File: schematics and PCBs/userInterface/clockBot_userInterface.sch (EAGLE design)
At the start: 6 parts, among them X1 5566-8

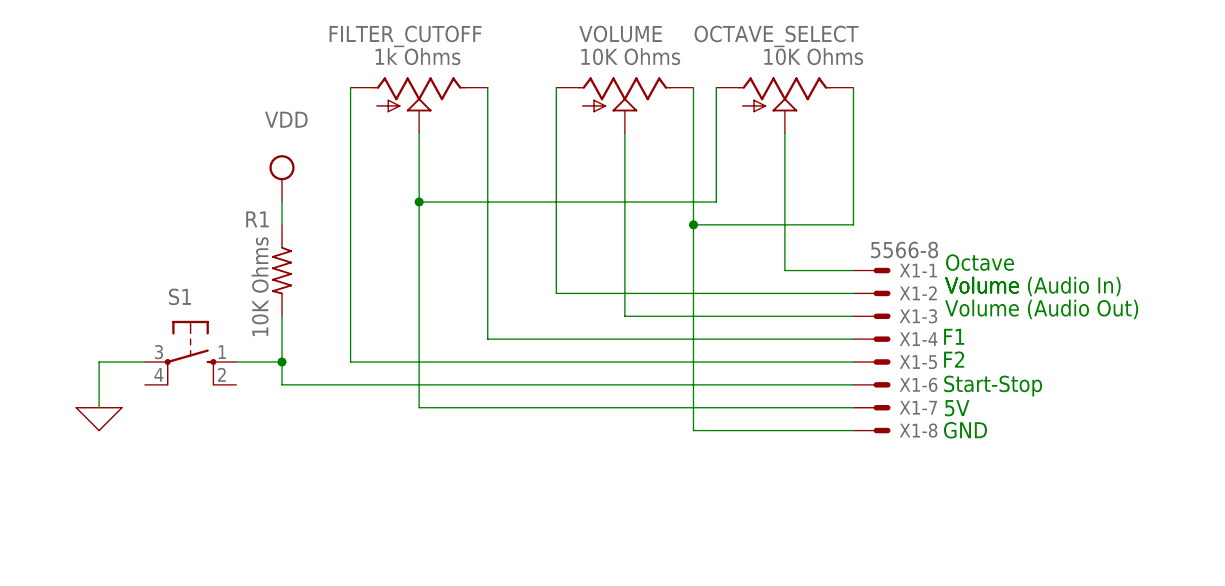
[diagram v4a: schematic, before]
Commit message: User itnerface switch update
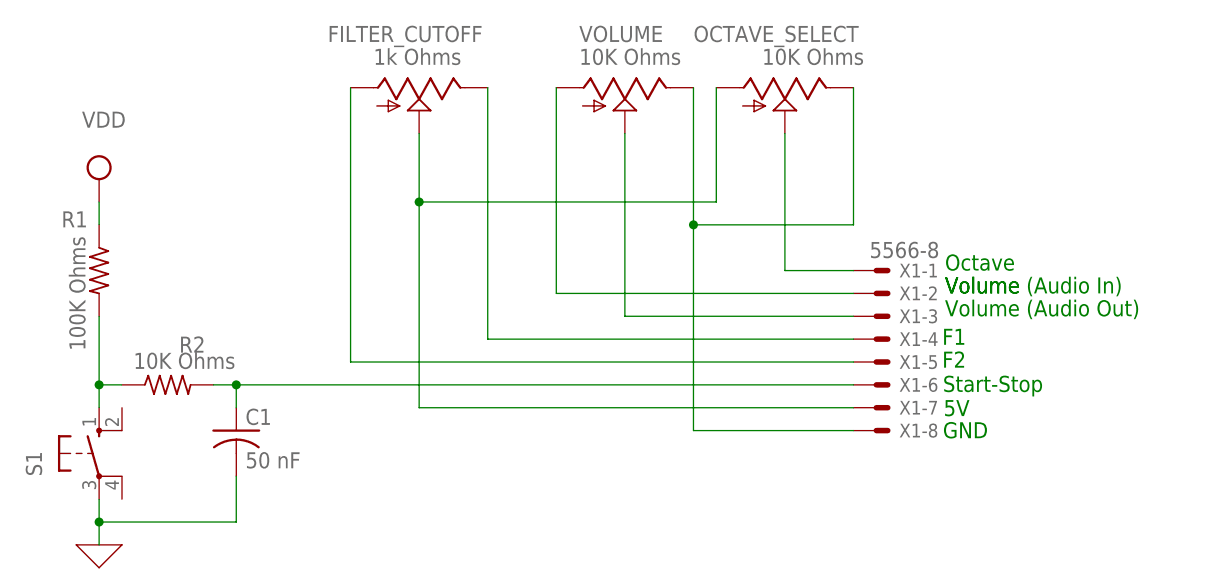
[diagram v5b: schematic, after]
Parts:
- added C1: 50 nF, adafruit:C-US025-025X050
- added R2: 10K Ohms, adafruit:FLIPFLOP-RES
- R1: value 10K Ohms -> 100K Ohms
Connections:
- new net N$7: R1.2, R2.1, S1.S
- net 0: now also C1.2
- net N$1: now also C1.1, R2.2; no longer R1.2, S1.S
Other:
- moved on the sheet: R1, S1
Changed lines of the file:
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@@
 <part name="SUPPLY1" library="supply2" library_urn="urn:adsk.eagle:library:372" deviceset="VDD" device=""/>
 <part name="X_1" library="ngspice-simulation" library_urn="urn:adsk.eagle:library:527439" deviceset="GND" device=""/>
-<part name="R1" library="adafruit" library_urn="urn:adsk.eagle:library:420" deviceset="FLIPFLOP-RES" device="" package3d_urn="urn:adsk.eagle:package:6240726/1" value="10K Ohms"/>
+<part name="R1" library="adafruit" library_urn="urn:adsk.eagle:library:420" deviceset="FLIPFLOP-RES" device="" package3d_urn="urn:adsk.eagle:package:6240726/1" value="100K Ohms"/>
 <part name="X1" library="con-molex" library_urn="urn:adsk.eagle:library:165" deviceset="5566-8" device="" package3d_urn="urn:adsk.eagle:package:8078580/1"/>
 <part name="S1" library="switch-omron" library_urn="urn:adsk.eagle:library:377" deviceset="10-XX" device="" package3d_urn="urn:adsk.eagle:package:27496/1"/>
+<part name="C1" library="adafruit" library_urn="urn:adsk.eagle:library:420" deviceset="C-US" device="025-025X050" package3d_urn="urn:adsk.eagle:package:6240323/1" value="50 nF"/>
+<part name="R2" library="adafruit" library_urn="urn:adsk.eagle:library:420" deviceset="FLIPFLOP-RES" device="" package3d_urn="urn:adsk.eagle:package:6240726/1" value="10K Ohms"/>
 </parts>
 <sheets>
@@
 <attribute name="VALUE" x="60.96" y="63.5" size="1.778" layer="96"/>
 </instance>
-<instance part="SUPPLY1" gate="G$1" x="7.62" y="50.8" smashed="yes">
-<attribute name="VALUE" x="5.715" y="56.515" size="1.778" layer="96"/>
+<instance part="SUPPLY1" gate="G$1" x="-12.7" y="50.8" smashed="yes">
+<attribute name="VALUE" x="-14.605" y="56.515" size="1.778" layer="96"/>
 </instance>
-<instance part="X_1" gate="G$1" x="-12.7" y="25.4" smashed="yes"/>
-<instance part="R1" gate="G$1" x="7.62" y="40.64" smashed="yes" rot="R270">
-<attribute name="NAME" x="6.35" y="47.2186" size="1.778" layer="95" rot="R180"/>
-<attribute name="VALUE" x="4.318" y="44.45" size="1.778" layer="96" rot="R270"/>
+<instance part="X_1" gate="G$1" x="-12.7" y="10.16" smashed="yes"/>
+<instance part="R1" gate="G$1" x="-12.7" y="40.64" smashed="yes" rot="R270">
+<attribute name="NAME" x="-13.97" y="47.2186" size="1.778" layer="95" rot="R180"/>
+<attribute name="VALUE" x="-16.002" y="44.45" size="1.778" layer="96" rot="R270"/>
 </instance>
 <instance part="X1" gate="-1" x="73.66" y="40.64" smashed="yes">
@@
 <attribute name="NAME" x="76.2" y="22.098" size="1.524" layer="95"/>
 </instance>
-<instance part="S1" gate="1" x="-2.54" y="30.48" smashed="yes" rot="R270">
-<attribute name="NAME" x="-5.08" y="36.83" size="1.778" layer="95"/>
-<attribute name="VALUE" x="0.635" y="34.29" size="1.778" layer="96"/>
+<instance part="S1" gate="1" x="-12.7" y="20.32" smashed="yes">
+<attribute name="NAME" x="-19.05" y="17.78" size="1.778" layer="95" rot="R90"/>
+<attribute name="VALUE" x="-16.51" y="23.495" size="1.778" layer="96" rot="R90"/>
+</instance>
+<instance part="C1" gate="G$1" x="2.54" y="22.86" smashed="yes">
+<attribute name="NAME" x="3.556" y="23.495" size="1.778" layer="95"/>
+<attribute name="VALUE" x="3.556" y="18.669" size="1.778" layer="96"/>
+</instance>
+<instance part="R2" gate="G$1" x="-5.08" y="27.94" smashed="yes">
+<attribute name="NAME" x="-3.81" y="31.5214" size="1.778" layer="95"/>
+<attribute name="VALUE" x="-8.89" y="29.718" size="1.778" layer="96"/>
 </instance>
 </instances>
@@
 </segment>
 </net>
-<net name="N$1" class="0">
-<segment>
-<pinref part="R1" gate="G$1" pin="2"/>
-<wire x1="7.62" y1="35.56" x2="7.62" y2="30.48" width="0.1524" layer="91"/>
-<wire x1="2.54" y1="30.48" x2="7.62" y2="30.48" width="0.1524" layer="91"/>
-<pinref part="X1" gate="-6" pin="S"/>
-<wire x1="71.12" y1="27.94" x2="7.62" y2="27.94" width="0.1524" layer="91"/>
-<wire x1="7.62" y1="27.94" x2="7.62" y2="30.48" width="0.1524" layer="91"/>
-<junction x="7.62" y="30.48"/>
-<pinref part="S1" gate="1" pin="S"/>
-</segment>
-</net>
 <net name="N$5" class="0">
 <segment>
@@
 <pinref part="R1" gate="G$1" pin="1"/>
 <pinref part="SUPPLY1" gate="G$1" pin="VDD"/>
-<wire x1="7.62" y1="48.26" x2="7.62" y2="45.72" width="0.1524" layer="91"/>
-</segment>
-</net>
-<net name="0" class="0">
-<segment>
-<wire x1="-12.7" y1="25.4" x2="-12.7" y2="30.48" width="0.1524" layer="91"/>
-<pinref part="X_1" gate="G$1" pin="0"/>
-<wire x1="-7.62" y1="30.48" x2="-12.7" y2="30.48" width="0.1524" layer="91"/>
-<pinref part="S1" gate="1" pin="P"/>
+<wire x1="-12.7" y1="48.26" x2="-12.7" y2="45.72" width="0.1524" layer="91"/>
 </segment>
 </net>
@@
 </segment>
 </net>
+<net name="0" class="0">
+<segment>
+<pinref part="X_1" gate="G$1" pin="0"/>
+<pinref part="S1" gate="1" pin="P"/>
+<wire x1="-12.7" y1="15.24" x2="-12.7" y2="12.7" width="0.1524" layer="91"/>
+<wire x1="-12.7" y1="12.7" x2="2.54" y2="12.7" width="0.1524" layer="91"/>
+<junction x="-12.7" y="12.7"/>
+<wire x1="-12.7" y1="12.7" x2="-12.7" y2="10.16" width="0.1524" layer="91"/>
+<pinref part="C1" gate="G$1" pin="2"/>
+<wire x1="2.54" y1="17.78" x2="2.54" y2="12.7" width="0.1524" layer="91"/>
+</segment>
+</net>
+<net name="N$1" class="0">
+<segment>
+<pinref part="X1" gate="-6" pin="S"/>
+<wire x1="71.12" y1="27.94" x2="2.54" y2="27.94" width="0.1524" layer="91"/>
+<pinref part="C1" gate="G$1" pin="1"/>
+<wire x1="2.54" y1="25.4" x2="2.54" y2="27.94" width="0.1524" layer="91"/>
+<pinref part="R2" gate="G$1" pin="2"/>
+<wire x1="0" y1="27.94" x2="2.54" y2="27.94" width="0.1524" layer="91"/>
+<junction x="2.54" y="27.94"/>
+</segment>
+</net>
+<net name="N$7" class="0">
+<segment>
+<pinref part="R1" gate="G$1" pin="2"/>
+<wire x1="-12.7" y1="35.56" x2="-12.7" y2="27.94" width="0.1524" layer="91"/>
+<pinref part="S1" gate="1" pin="S"/>
+<pinref part="R2" gate="G$1" pin="1"/>
+<wire x1="-12.7" y1="27.94" x2="-12.7" y2="25.4" width="0.1524" layer="91"/>
+<wire x1="-10.16" y1="27.94" x2="-12.7" y2="27.94" width="0.1524" layer="91"/>
+<junction x="-12.7" y="27.94"/>
+</segment>
+</net>

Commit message: User interface single row molex
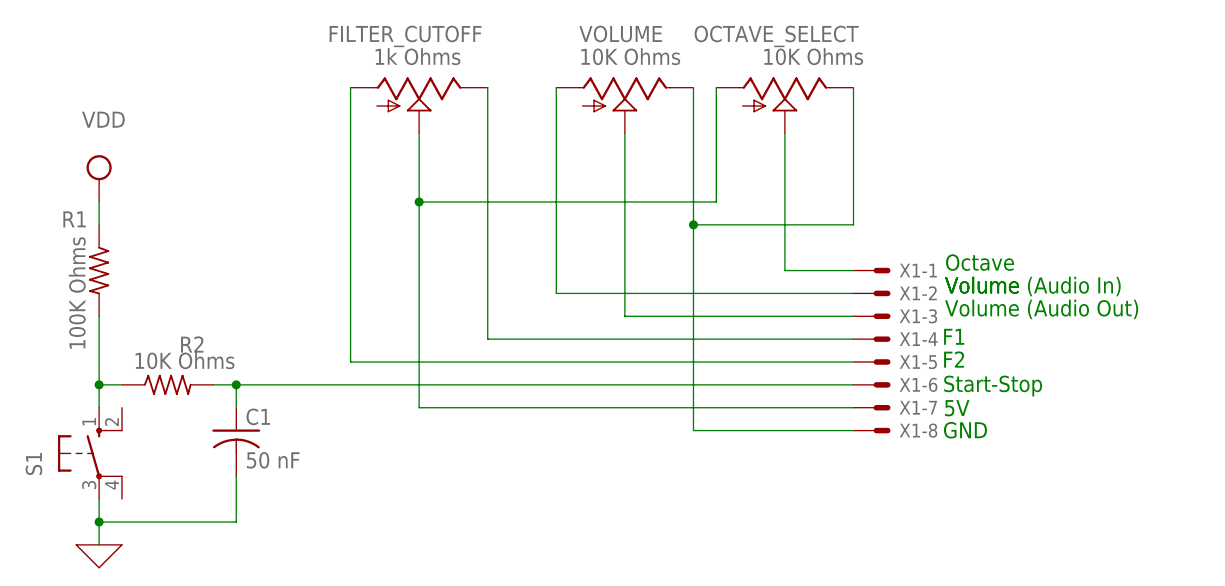
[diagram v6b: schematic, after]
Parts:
- X1: value 5566-8 -> (none); device con-molex:5566-8 -> con-molex:KK-156-8
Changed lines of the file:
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@@
 <part name="X_1" library="ngspice-simulation" library_urn="urn:adsk.eagle:library:527439" deviceset="GND" device=""/>
 <part name="R1" library="adafruit" library_urn="urn:adsk.eagle:library:420" deviceset="FLIPFLOP-RES" device="" package3d_urn="urn:adsk.eagle:package:6240726/1" value="100K Ohms"/>
-<part name="X1" library="con-molex" library_urn="urn:adsk.eagle:library:165" deviceset="5566-8" device="" package3d_urn="urn:adsk.eagle:package:8078580/1"/>
 <part name="S1" library="switch-omron" library_urn="urn:adsk.eagle:library:377" deviceset="10-XX" device="" package3d_urn="urn:adsk.eagle:package:27496/1"/>
 <part name="C1" library="adafruit" library_urn="urn:adsk.eagle:library:420" deviceset="C-US" device="025-025X050" package3d_urn="urn:adsk.eagle:package:6240323/1" value="50 nF"/>
 <part name="R2" library="adafruit" library_urn="urn:adsk.eagle:library:420" deviceset="FLIPFLOP-RES" device="" package3d_urn="urn:adsk.eagle:package:6240726/1" value="10K Ohms"/>
+<part name="X1" library="con-molex" library_urn="urn:adsk.eagle:library:165" deviceset="KK-156-8" device="" package3d_urn="urn:adsk.eagle:package:8078814/1"/>
 </parts>
 <sheets>
@@
 <attribute name="VALUE" x="-16.002" y="44.45" size="1.778" layer="96" rot="R270"/>
 </instance>
+<instance part="S1" gate="1" x="-12.7" y="20.32" smashed="yes">
+<attribute name="NAME" x="-19.05" y="17.78" size="1.778" layer="95" rot="R90"/>
+<attribute name="VALUE" x="-16.51" y="23.495" size="1.778" layer="96" rot="R90"/>
+</instance>
+<instance part="C1" gate="G$1" x="2.54" y="22.86" smashed="yes">
+<attribute name="NAME" x="3.556" y="23.495" size="1.778" layer="95"/>
+<attribute name="VALUE" x="3.556" y="18.669" size="1.778" layer="96"/>
+</instance>
+<instance part="R2" gate="G$1" x="-5.08" y="27.94" smashed="yes">
+<attribute name="NAME" x="-3.81" y="31.5214" size="1.778" layer="95"/>
+<attribute name="VALUE" x="-8.89" y="29.718" size="1.778" layer="96"/>
+</instance>
 <instance part="X1" gate="-1" x="73.66" y="40.64" smashed="yes">
 <attribute name="NAME" x="76.2" y="39.878" size="1.524" layer="95"/>
@@
 <attribute name="NAME" x="76.2" y="22.098" size="1.524" layer="95"/>
 </instance>
-<instance part="S1" gate="1" x="-12.7" y="20.32" smashed="yes">
-<attribute name="NAME" x="-19.05" y="17.78" size="1.778" layer="95" rot="R90"/>
-<attribute name="VALUE" x="-16.51" y="23.495" size="1.778" layer="96" rot="R90"/>
-</instance>
-<instance part="C1" gate="G$1" x="2.54" y="22.86" smashed="yes">
-<attribute name="NAME" x="3.556" y="23.495" size="1.778" layer="95"/>
-<attribute name="VALUE" x="3.556" y="18.669" size="1.778" layer="96"/>
-</instance>
-<instance part="R2" gate="G$1" x="-5.08" y="27.94" smashed="yes">
-<attribute name="NAME" x="-3.81" y="31.5214" size="1.778" layer="95"/>
-<attribute name="VALUE" x="-8.89" y="29.718" size="1.778" layer="96"/>
-</instance>
 </instances>
 <busses>
@@
 <pinref part="FILTER_CUTOFF" gate="G$1" pin="E"/>
 <wire x1="30.48" y1="60.96" x2="30.48" y2="33.02" width="0.1524" layer="91"/>
+<wire x1="30.48" y1="33.02" x2="71.12" y2="33.02" width="0.1524" layer="91"/>
 <pinref part="X1" gate="-4" pin="S"/>
-<wire x1="30.48" y1="33.02" x2="71.12" y2="33.02" width="0.1524" layer="91"/>
 </segment>
 </net>
@@
 <pinref part="VOLUME" gate="G$1" pin="S"/>
 <wire x1="45.72" y1="55.88" x2="45.72" y2="35.56" width="0.1524" layer="91"/>
+<wire x1="45.72" y1="35.56" x2="71.12" y2="35.56" width="0.1524" layer="91"/>
 <pinref part="X1" gate="-3" pin="S"/>
-<wire x1="45.72" y1="35.56" x2="71.12" y2="35.56" width="0.1524" layer="91"/>
 </segment>
 </net>
@@
 <pinref part="FILTER_CUTOFF" gate="G$1" pin="A"/>
 <wire x1="15.24" y1="60.96" x2="15.24" y2="30.48" width="0.1524" layer="91"/>
+<wire x1="71.12" y1="30.48" x2="15.24" y2="30.48" width="0.1524" layer="91"/>
 <pinref part="X1" gate="-5" pin="S"/>
-<wire x1="71.12" y1="30.48" x2="15.24" y2="30.48" width="0.1524" layer="91"/>
 </segment>
 </net>
@@
 <wire x1="22.86" y1="48.26" x2="22.86" y2="25.4" width="0.1524" layer="91"/>
 <junction x="22.86" y="48.26"/>
+<wire x1="71.12" y1="25.4" x2="22.86" y2="25.4" width="0.1524" layer="91"/>
 <pinref part="X1" gate="-7" pin="S"/>
-<wire x1="71.12" y1="25.4" x2="22.86" y2="25.4" width="0.1524" layer="91"/>
 </segment>
 </net>
@@
 <wire x1="53.34" y1="45.72" x2="53.34" y2="22.86" width="0.1524" layer="91"/>
 <junction x="53.34" y="45.72"/>
+<wire x1="53.34" y1="22.86" x2="71.12" y2="22.86" width="0.1524" layer="91"/>
 <pinref part="X1" gate="-8" pin="S"/>
-<wire x1="53.34" y1="22.86" x2="71.12" y2="22.86" width="0.1524" layer="91"/>
 </segment>
 </net>
@@
 <segment>
 <pinref part="VOLUME" gate="G$1" pin="A"/>
-<pinref part="X1" gate="-2" pin="S"/>
 <wire x1="38.1" y1="60.96" x2="38.1" y2="38.1" width="0.1524" layer="91"/>
 <wire x1="38.1" y1="38.1" x2="71.12" y2="38.1" width="0.1524" layer="91"/>
+<pinref part="X1" gate="-2" pin="S"/>
 </segment>
 </net>
@@
 <net name="N$1" class="0">
 <segment>
-<pinref part="X1" gate="-6" pin="S"/>
 <wire x1="71.12" y1="27.94" x2="2.54" y2="27.94" width="0.1524" layer="91"/>
 <pinref part="C1" gate="G$1" pin="1"/>
@@
 <wire x1="0" y1="27.94" x2="2.54" y2="27.94" width="0.1524" layer="91"/>
 <junction x="2.54" y="27.94"/>
+<pinref part="X1" gate="-6" pin="S"/>
 </segment>
 </net>
